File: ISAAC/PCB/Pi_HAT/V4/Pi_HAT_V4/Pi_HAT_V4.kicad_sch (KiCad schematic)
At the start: 7 parts, among them J1 MPU 6050, J2 Pi_GPIO, J3 Display

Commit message: Updated code: Sorta works
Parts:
- added J7: Pressure Sensor, Connector_PinHeader_2.54mm:PinHeader_1x03_P2.54mm_Vertical, symbol Connector_Generic:Conn_01x03
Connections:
- net 5V: now also J7.1 (Pin_1)
- net GND: now also J7.2 (Pin_2)
- net MOSI: now reaches J2.19 (Pin_19)
- net MISO: now reaches J2.21 (Pin_21)
- net SCLK: now reaches J2.23 (Pin_23)
- net CS: now reaches J2.24 (Pin_24)
- new net PS: J7.3 (Pin_3)
- no-connect marks 36 -> 32
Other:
- added sheet A-D Converter (A-D Converter.kicad_sch)
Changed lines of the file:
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@@
 (kicad_sch (version 20230121) (generator eeschema)
   (paper "A4")
-  (no_connect (at 112.776 87.884))
   (no_connect (at 125.476 80.264))
   (no_connect (at 125.476 82.804))
@@
   (no_connect (at 112.776 108.204))
   (no_connect (at 125.476 85.344))
-  (no_connect (at 125.476 90.424))
-  (no_connect (at 112.776 90.424))
   (no_connect (at 112.776 70.104))
   (no_connect (at 125.476 95.504))
@@
   (no_connect (at 125.476 105.664))
   (no_connect (at 112.776 105.664))
-  (no_connect (at 112.776 85.344))
   (no_connect (at 112.776 77.724))
   (wire (pts (xy 125.476 67.564) (xy 128.651 67.564))
@@
     (stroke (width 0) (type default))
   )
+  (wire (pts (xy 108.204 90.424) (xy 112.776 90.424))
+    (stroke (width 0) (type default))
+  )
   (wire (pts (xy 141.986 59.69) (xy 137.16 59.69))
     (stroke (width 0) (type default))
@@
     (stroke (width 0) (type default))
   )
+  (wire (pts (xy 182.626 123.19) (xy 187.198 123.19))
+    (stroke (width 0) (type default))
+  )
   (wire (pts (xy 107.696 67.564) (xy 112.776 67.564))
     (stroke (width 0) (type default))
@@
     (stroke (width 0) (type default))
   )
+  (wire (pts (xy 182.626 120.904) (xy 187.198 120.904))
+    (stroke (width 0) (type default))
+  )
   (wire (pts (xy 128.778 65.024) (xy 125.476 65.024))
     (stroke (width 0) (type default))
   )
+  (wire (pts (xy 182.626 127.762) (xy 187.198 127.762))
+    (stroke (width 0) (type default))
+  )
   (wire (pts (xy 137.16 80.772) (xy 143.51 80.772))
     (stroke (width 0) (type default))
   )
+  (wire (pts (xy 182.118 134.62) (xy 187.198 134.62))
+    (stroke (width 0) (type default))
+  )
   (wire (pts (xy 183.388 78.486) (xy 187.452 78.486))
     (stroke (width 0) (type default))
   )
+  (wire (pts (xy 182.626 125.476) (xy 187.198 125.476))
+    (stroke (width 0) (type default))
+  )
   (wire (pts (xy 107.696 65.024) (xy 112.776 65.024))
     (stroke (width 0) (type default))
   )
+  (wire (pts (xy 125.476 90.424) (xy 130.048 90.424))
+    (stroke (width 0) (type default))
+  )
+  (wire (pts (xy 108.204 87.884) (xy 112.776 87.884))
+    (stroke (width 0) (type default))
+  )
+  (wire (pts (xy 182.626 130.048) (xy 187.198 130.048))
+    (stroke (width 0) (type default))
+  )
+  (wire (pts (xy 153.924 99.822) (xy 159.004 99.822))
+    (stroke (width 0) (type default))
+  )
   (wire (pts (xy 141.986 57.15) (xy 141.986 56.134))
     (stroke (width 0) (type default))
@@
     (stroke (width 0) (type default))
   )
+  (wire (pts (xy 153.924 94.742) (xy 159.004 94.742))
+    (stroke (width 0) (type default))
+  )
   (wire (pts (xy 128.778 62.484) (xy 125.476 62.484))
     (stroke (width 0) (type default))
@@
     (stroke (width 0) (type default))
   )
+  (wire (pts (xy 108.204 85.344) (xy 112.776 85.344))
+    (stroke (width 0) (type default))
+  )
   (wire (pts (xy 157.988 57.15) (xy 154.686 57.15))
     (stroke (width 0) (type default))
   )
+  (wire (pts (xy 182.626 132.334) (xy 187.198 132.334))
+    (stroke (width 0) (type default))
+  )
+  (wire (pts (xy 182.118 137.16) (xy 187.198 137.16))
+    (stroke (width 0) (type default))
+  )
   (label "5V" (at 128.778 65.024 180) (fields_autoplaced)
     (effects (font (size 1.27 1.27)) (justify right bottom))
   )
+  (label "MOSI" (at 108.204 85.344 0) (fields_autoplaced)
+    (effects (font (size 1.27 1.27)) (justify left bottom))
+  )
   (label "3.3V" (at 137.16 73.152 0) (fields_autoplaced)
     (effects (font (size 1.27 1.27)) (justify left bottom))
   )
+  (label "3.3V" (at 182.626 120.904 0) (fields_autoplaced)
+    (effects (font (size 1.27 1.27)) (justify left bottom))
+  )
   (label "3.3V" (at 141.986 56.134 180) (fields_autoplaced)
     (effects (font (size 1.27 1.27)) (justify right bottom))
@@
     (effects (font (size 1.27 1.27)) (justify left bottom))
   )
+  (label "PS" (at 182.626 132.334 0) (fields_autoplaced)
+    (effects (font (size 1.27 1.27)) (justify left bottom))
+  )
+  (label "SCLK" (at 108.204 90.424 0) (fields_autoplaced)
+    (effects (font (size 1.27 1.27)) (justify left bottom))
+  )
+  (label "12V0" (at 182.118 134.62 0) (fields_autoplaced)
+    (effects (font (size 1.27 1.27)) (justify left bottom))
+  )
+  (label "CS" (at 182.626 130.048 0) (fields_autoplaced)
+    (effects (font (size 1.27 1.27)) (justify left bottom))
+  )
   (label "5V" (at 157.988 59.69 180) (fields_autoplaced)
     (effects (font (size 1.27 1.27)) (justify right bottom))
   )
+  (label "CS" (at 130.048 90.424 180) (fields_autoplaced)
+    (effects (font (size 1.27 1.27)) (justify right bottom))
+  )
+  (label "MOSI" (at 182.626 125.476 0) (fields_autoplaced)
+    (effects (font (size 1.27 1.27)) (justify left bottom))
+  )
+  (label "PS" (at 159.004 94.742 180) (fields_autoplaced)
+    (effects (font (size 1.27 1.27)) (justify right bottom))
+  )
+  (label "12V1" (at 182.118 137.16 0) (fields_autoplaced)
+    (effects (font (size 1.27 1.27)) (justify left bottom))
+  )
+  (label "MISO" (at 182.626 123.19 0) (fields_autoplaced)
+    (effects (font (size 1.27 1.27)) (justify left bottom))
+  )
   (label "SCL" (at 137.16 80.772 0) (fields_autoplaced)
     (effects (font (size 1.27 1.27)) (justify left bottom))
@@
     (effects (font (size 1.27 1.27)) (justify left bottom))
   )
+  (label "MISO" (at 108.204 87.884 0) (fields_autoplaced)
+    (effects (font (size 1.27 1.27)) (justify left bottom))
+  )
   (label "5V" (at 157.988 57.15 180) (fields_autoplaced)
     (effects (font (size 1.27 1.27)) (justify right bottom))
   )
+  (label "SCLK" (at 182.626 127.762 0) (fields_autoplaced)
+    (effects (font (size 1.27 1.27)) (justify left bottom))
+  )
   (label "12V0" (at 182.372 84.328 0) (fields_autoplaced)
     (effects (font (size 1.27 1.27)) (justify left bottom))
   )
   (label "5V" (at 128.778 62.484 180) (fields_autoplaced)
+    (effects (font (size 1.27 1.27)) (justify right bottom))
+  )
+  (label "5V" (at 159.004 99.822 180) (fields_autoplaced)
     (effects (font (size 1.27 1.27)) (justify right bottom))
   )
@@
     )
   )
+  (symbol (lib_id "power:GND") (at 153.924 97.282 90) (unit 1)
+    (in_bom yes) (on_board yes) (dnp no)
+    (property "Reference" "#PWR0111" (at 160.274 97.282 0)
+      (effects (font (size 1.27 1.27)) hide)
+    )
+    (property "Value" "GND" (at 156.464 97.282 90)
+      (effects (font (size 1.27 1.27)) (justify right))
+    )
+    (property "Footprint" "" (at 153.924 97.282 0)
+      (effects (font (size 1.27 1.27)) hide)
+    )
+    (property "Datasheet" "" (at 153.924 97.282 0)
+      (effects (font (size 1.27 1.27)) hide)
+    )
+    (pin "1")
+    (instances
+      (project "Pi_HAT_V4"
+        (path "/e63e39d7-6ac0-4ffd-8aa3-1841a4541b55"
+          (reference "#PWR0111") (unit 1)
+        )
+      )
+    )
+  )
+  (symbol (lib_id "Connector_Generic:Conn_01x03") (at 148.844 97.282 180) (unit 1)
+    (in_bom yes) (on_board yes) (dnp no) (fields_autoplaced)
+    (property "Reference" "J7" (at 148.844 88.392 0)
+      (effects (font (size 1.27 1.27)))
+    )
+    (property "Value" "Pressure Sensor" (at 148.844 90.932 0)
+      (effects (font (size 1.27 1.27)))
+    )
+    (property "Footprint" "Connector_PinHeader_2.54mm:PinHeader_1x03_P2.54mm_Vertical" (at 148.844 97.282 0)
+      (effects (font (size 1.27 1.27)) hide)
+    )
+    (property "Datasheet" "https://www.te.com/commerce/DocumentDelivery/DDEController?Action=srchrtrv&DocNm=MSP340&DocType=Data+Sheet&DocLang=English" (at 148.844 97.282 0)
+      (effects (font (size 1.27 1.27)) hide)
+    )
+    (pin "1")
+    (pin "2")
+    (pin "3")
+    (instances
+      (project "Pi_HAT_V4"
+        (path "/e63e39d7-6ac0-4ffd-8aa3-1841a4541b55"
+          (reference "J7") (unit 1)
+        )
+      )
+    )
+  )
   (sheet (at 187.452 61.976) (size 68.326 39.878) (fields_autoplaced)
     (stroke (width 0) (type solid))
@@
       )
     )
+  )
+  (sheet (at 187.198 116.332) (size 68.834 31.242) (fields_autoplaced)
+    (stroke (width 0.1524) (type solid))
+    (fill (color 0 0 0 0.0000))
+    (property "Sheetname" "A-D Converter" (at 187.198 115.6204 0)
+      (effects (font (size 1.27 1.27)) (justify left bottom))
+    )
+    (property "Sheetfile" "A-D Converter.kicad_sch" (at 187.198 148.1586 0)
+      (effects (font (size 1.27 1.27)) (justify left top))
+    )
+    (pin "3.3V" input (at 187.198 120.904 180)
+      (effects (font (size 1.27 1.27)) (justify left))
+    )
+    (pin "MISO" input (at 187.198 123.19 180)
+      (effects (font (size 1.27 1.27)) (justify left))
+    )
+    (pin "MOSI" input (at 187.198 125.476 180)
+      (effects (font (size 1.27 1.27)) (justify left))
+    )
+    (pin "SCLK" input (at 187.198 127.762 180)
+      (effects (font (size 1.27 1.27)) (justify left))
+    )
+    (pin "CS" input (at 187.198 130.048 180)
+      (effects (font (size 1.27 1.27)) (justify left))
+    )
+    (pin "PS" input (at 187.198 132.334 180)
+      (effects (font (size 1.27 1.27)) (justify left))
+    )
+    (pin "VCC0" input (at 187.198 134.62 180)
+      (effects (font (size 1.27 1.27)) (justify left))
+    )
+    (pin "VCC1" input (at 187.198 137.16 180)
+      (effects (font (size 1.27 1.27)) (justify left))
+    )
+    (instances
+      (project "Pi_HAT_V4"
+        (path "/e63e39d7-6ac0-4ffd-8aa3-1841a4541b55" (page "3"))
+      )
+    )

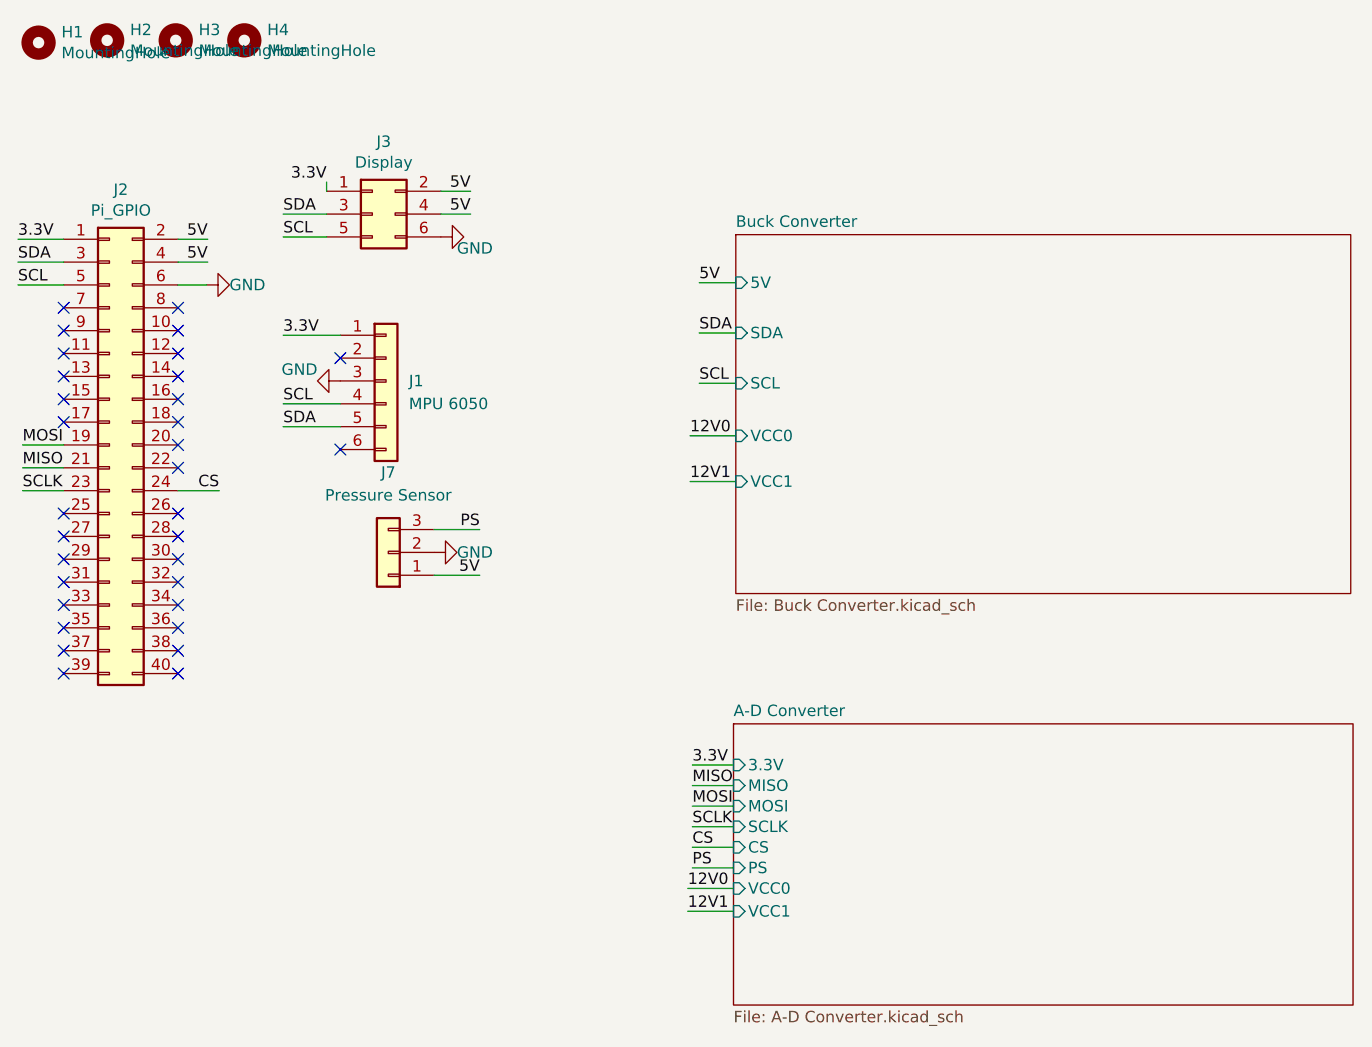
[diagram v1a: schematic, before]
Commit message: Updated
Started SPARK grant and updated controller and PCB
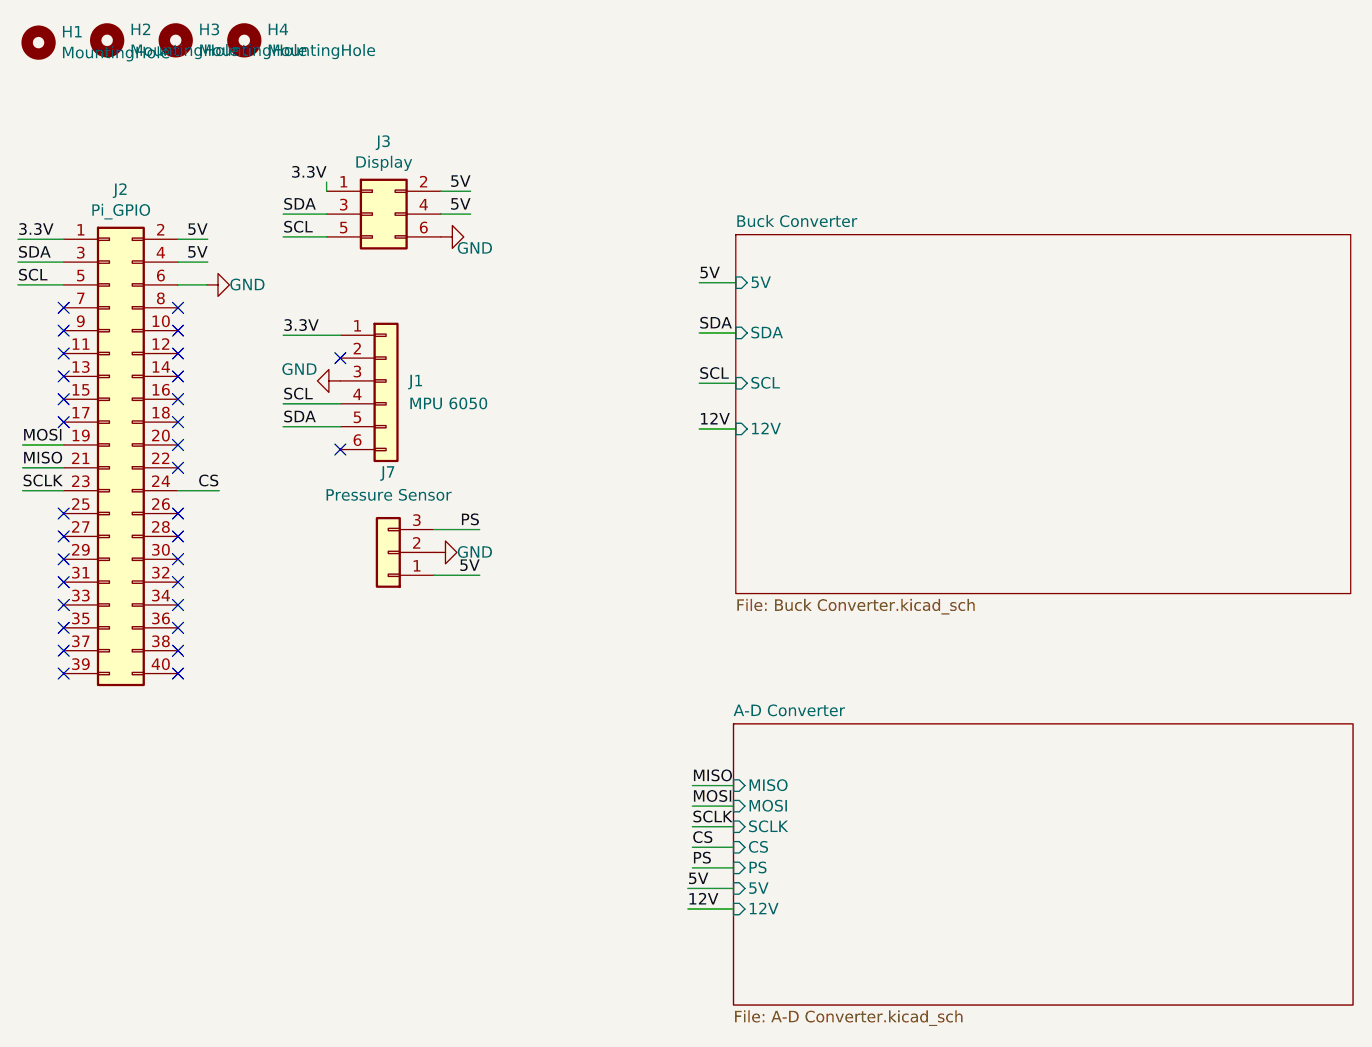
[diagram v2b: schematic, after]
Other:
- sheet A-D Converter ports: added 12V, 5V; removed 3.3V, VCC0, VCC1
- sheet Buck Converter ports: added 12V; removed VCC0, VCC1
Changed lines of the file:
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@@
+    (stroke (width 0) (type default))
+  )
+  (wire (pts (xy 182.118 136.906) (xy 187.198 136.906))
     (stroke (width 0) (type default))
   )
@@
     (stroke (width 0) (type default))
   )
-  (wire (pts (xy 182.372 89.408) (xy 187.452 89.408))
-    (stroke (width 0) (type default))
-  )
   (wire (pts (xy 137.16 83.312) (xy 143.51 83.312))
     (stroke (width 0) (type default))
@@
     (stroke (width 0) (type default))
   )
-  (wire (pts (xy 182.626 120.904) (xy 187.198 120.904))
-    (stroke (width 0) (type default))
-  )
   (wire (pts (xy 128.778 65.024) (xy 125.476 65.024))
     (stroke (width 0) (type default))
@@
     (stroke (width 0) (type default))
   )
+  (wire (pts (xy 183.388 83.566) (xy 187.452 83.566))
+    (stroke (width 0) (type default))
+  )
   (wire (pts (xy 183.388 72.898) (xy 187.452 72.898))
     (stroke (width 0) (type default))
@@
     (stroke (width 0) (type default))
   )
-  (wire (pts (xy 182.372 84.328) (xy 187.452 84.328))
-    (stroke (width 0) (type default))
-  )
   (wire (pts (xy 108.204 85.344) (xy 112.776 85.344))
     (stroke (width 0) (type default))
@@
     (stroke (width 0) (type default))
   )
-  (wire (pts (xy 182.118 137.16) (xy 187.198 137.16))
-    (stroke (width 0) (type default))
-  )
   (label "5V" (at 128.778 65.024 180) (fields_autoplaced)
     (effects (font (size 1.27 1.27)) (justify right bottom))
@@
     (effects (font (size 1.27 1.27)) (justify left bottom))
   )
-  (label "3.3V" (at 182.626 120.904 0) (fields_autoplaced)
-    (effects (font (size 1.27 1.27)) (justify left bottom))
-  )
   (label "3.3V" (at 141.986 56.134 180) (fields_autoplaced)
     (effects (font (size 1.27 1.27)) (justify right bottom))
   )
-  (label "12V1" (at 182.372 89.408 0) (fields_autoplaced)
-    (effects (font (size 1.27 1.27)) (justify left bottom))
-  )
   (label "SDA" (at 107.696 65.024 0) (fields_autoplaced)
     (effects (font (size 1.27 1.27)) (justify left bottom))
@@
     (effects (font (size 1.27 1.27)) (justify left bottom))
   )
-  (label "12V0" (at 182.118 134.62 0) (fields_autoplaced)
+  (label "5V" (at 182.118 134.62 0) (fields_autoplaced)
     (effects (font (size 1.27 1.27)) (justify left bottom))
   )
@@
     (effects (font (size 1.27 1.27)) (justify right bottom))
   )
-  (label "12V1" (at 182.118 137.16 0) (fields_autoplaced)
-    (effects (font (size 1.27 1.27)) (justify left bottom))
-  )
   (label "MISO" (at 182.626 123.19 0) (fields_autoplaced)
     (effects (font (size 1.27 1.27)) (justify left bottom))
@@
     (effects (font (size 1.27 1.27)) (justify left bottom))
   )
+  (label "12V" (at 182.118 136.906 0) (fields_autoplaced)
+    (effects (font (size 1.27 1.27)) (justify left bottom))
+  )
   (label "SDA" (at 137.16 59.69 0) (fields_autoplaced)
     (effects (font (size 1.27 1.27)) (justify left bottom))
@@
     (effects (font (size 1.27 1.27)) (justify right bottom))
   )
+  (label "12V" (at 183.388 83.566 0) (fields_autoplaced)
+    (effects (font (size 1.27 1.27)) (justify left bottom))
+  )
   (label "SCLK" (at 182.626 127.762 0) (fields_autoplaced)
-    (effects (font (size 1.27 1.27)) (justify left bottom))
-  )
-  (label "12V0" (at 182.372 84.328 0) (fields_autoplaced)
     (effects (font (size 1.27 1.27)) (justify left bottom))
   )
@@
       (effects (font (size 1.27 1.27)) (justify left))
     )
-    (pin "VCC0" input (at 187.452 84.328 180)
-      (effects (font (size 1.27 1.27)) (justify left))
-    )
-    (pin "VCC1" input (at 187.452 89.408 180)
+    (pin "12V" input (at 187.452 83.566 180)
       (effects (font (size 1.27 1.27)) (justify left))
     )
@@
       (effects (font (size 1.27 1.27)) (justify left top))
     )
-    (pin "3.3V" input (at 187.198 120.904 180)
-      (effects (font (size 1.27 1.27)) (justify left))
-    )
     (pin "MISO" input (at 187.198 123.19 180)
       (effects (font (size 1.27 1.27)) (justify left))
@@
       (effects (font (size 1.27 1.27)) (justify left))
     )
-    (pin "VCC0" input (at 187.198 134.62 180)
-      (effects (font (size 1.27 1.27)) (justify left))
-    )
-    (pin "VCC1" input (at 187.198 137.16 180)
-      (effects (font (size 1.27 1.27)) (justify left))
-    )
+    (pin "5V" input (at 187.198 134.62 180)
+      (effects (font (size 1.27 1.27)) (justify left))
+    )
+    (pin "12V" input (at 187.198 136.906 180)
+      (effects (font (size 1.27 1.27)) (justify left))
+    )

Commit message: Updated ISAAC PCB
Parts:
- removed J1: MPU 6050, Connector_PinHeader_2.54mm:PinHeader_1x06_P2.54mm_Vertical, symbol 24V_Li_batt:Conn_01x06
- removed J7: Pressure Sensor, Connector_PinHeader_2.54mm:PinHeader_1x03_P2.54mm_Vertical, symbol Connector_Generic:Conn_01x03
- added J1: MPU 9250, Connector_PinHeader_2.54mm:PinHeader_1x10_P2.54mm_Vertical, symbol Connector_Generic:Conn_01x10
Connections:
- net 3.3V: now also J1.1 (Pin_1)
- net GND: now also J1.2 (Pin_2)
- net SCL: now also J1.3 (Pin_3)
- net SDA: now also J1.4 (Pin_4)
- no-connect marks 32 -> 36
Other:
- removed sheet A-D Converter
